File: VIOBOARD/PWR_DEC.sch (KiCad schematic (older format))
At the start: 4 parts

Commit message: Libraries modified as part of the BBB cape developement.
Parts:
- C26, C27, C28, C29: symbol device:C_Small -> VIOBOARD-rescue:C_Small-device
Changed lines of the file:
@@
 	1450 1350 2900 1350
 $Comp
-L device:C_Small C26
+L VIOBOARD-rescue:C_Small-device C26
 U 1 1 59569800
 P 1600 1550
@@
 $EndComp
 $Comp
-L device:C_Small C27
+L VIOBOARD-rescue:C_Small-device C27
 U 1 1 59569857
 P 1900 1550
@@
 $EndComp
 $Comp
-L device:C_Small C28
+L VIOBOARD-rescue:C_Small-device C28
 U 1 1 59569892
 P 2200 1550
@@
 $EndComp
 $Comp
-L device:C_Small C29
+L VIOBOARD-rescue:C_Small-device C29
 U 1 1 595698B3
 P 2500 1550

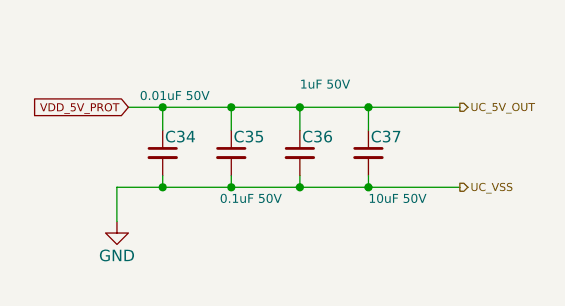
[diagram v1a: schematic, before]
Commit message: Schematics cleanup.  Gerbers for the latest manufacturing release.
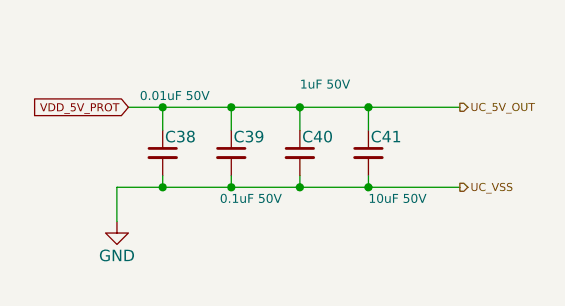
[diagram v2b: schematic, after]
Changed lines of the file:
@@
 UC_VSS
 Wire Wire Line
-	1400 1700 2900 1700
+	1400 1700 1600 1700
 Wire Wire Line
-	1450 1350 2900 1350
+	1450 1350 1600 1350
 $Comp
 L VIOBOARD-rescue:C_Small-device C26
@@
 AR Path="/59154FA7/595829B5/59569800" Ref="C34"  Part="1"
 AR Path="/59154FA7/5958475A/59569800" Ref="C38"  Part="1"
-F 0 "C34" H 1610 1620 50  0000 L CNN
+F 0 "C38" H 1610 1620 50  0000 L CNN
 F 1 "0.01uF 50V" H 1500 1800 39  0000 L CNN
 F 2 "Capacitors_SMD:C_0805" H 1600 1550 50  0001 C CNN
@@
 AR Path="/59154FA7/595829B5/59569857" Ref="C35"  Part="1"
 AR Path="/59154FA7/5958475A/59569857" Ref="C39"  Part="1"
-F 0 "C35" H 1910 1620 50  0000 L CNN
+F 0 "C39" H 1910 1620 50  0000 L CNN
 F 1 "0.1uF 50V" H 1850 1350 39  0000 L CNN
 F 2 "Capacitors_SMD:C_0805" H 1900 1550 50  0001 C CNN
@@
 AR Path="/59154FA7/595829B5/59569892" Ref="C36"  Part="1"
 AR Path="/59154FA7/5958475A/59569892" Ref="C40"  Part="1"
-F 0 "C36" H 2210 1620 50  0000 L CNN
+F 0 "C40" H 2210 1620 50  0000 L CNN
 F 1 "1uF 50V" H 2200 1850 39  0000 L CNN
 F 2 "Capacitors_SMD:C_0805" H 2200 1550 50  0001 C CNN
@@
 AR Path="/59154FA7/595829B5/595698B3" Ref="C37"  Part="1"
 AR Path="/59154FA7/5958475A/595698B3" Ref="C41"  Part="1"
-F 0 "C37" H 2510 1620 50  0000 L CNN
+F 0 "C41" H 2510 1620 50  0000 L CNN
 F 1 "10uF 50V" H 2500 1350 39  0000 L CNN
 F 2 "Capacitors_SMD:C_1206" H 2500 1550 50  0001 C CNN
@@
 Text GLabel 1450 1350 0    35   Input ~ 0
 VDD_5V_PROT
+Wire Wire Line
+	1600 1350 1900 1350
+Wire Wire Line
+	1600 1700 1900 1700
+Wire Wire Line
+	1900 1350 2200 1350
+Wire Wire Line
+	1900 1700 2200 1700
+Wire Wire Line
+	2200 1350 2500 1350
+Wire Wire Line
+	2200 1700 2500 1700
+Wire Wire Line
+	2500 1350 2900 1350
+Wire Wire Line
+	2500 1700 2900 1700
 $EndSCHEMATC
